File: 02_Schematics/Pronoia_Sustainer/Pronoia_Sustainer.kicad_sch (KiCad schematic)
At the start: 0 parts

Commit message: Initial start for Pronoia Schematic
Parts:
- added C1, C2: 10uF, symbol Device:C
- added C3, C4: 22uF, symbol Device:C
- added C5: 0.1uF, symbol Device:C
- added J1: J1_Bat, symbol Connector:Conn_01x02_Pin
- added J2: J2_Switch, symbol Connector:Conn_01x02_Pin
- added L1: 3.3uH, symbol Device:L
- added R1: 56.2k, symbol Device:R_US
- added R2: 10k, symbol Device:R_US
- added U1: TPS563201, Package_TO_SOT_SMD:SOT-23-6, symbol Regulator_Switching:TPS563201
- added U2: Teensy4.1, symbol teensy:Teensy4.1
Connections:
- new net: C1.1, C2.2, J2.2 (Pin_2), U1.3 (VIN), U1.5 (EN)
- new net: J1.1 (Pin_1), J2.1 (Pin_1)
- new net: R1.2, R2.1, U1.4 (VFB)
- new net: C5.1, L1.1, U1.2 (SW)
- new net: C5.2, U1.6 (VBST)
- new net +5V: C3.2, C4.1, L1.2, R1.1, U2.48 (VIN)
- new net GND: C1.2, C2.1, C3.1, C4.2, J1.2 (Pin_2), R2.2, U1.1 (GND), U2.47 (GND)
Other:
- company: (none) -> Walla Walla University
- title: (none) -> Pronoia Sustainer

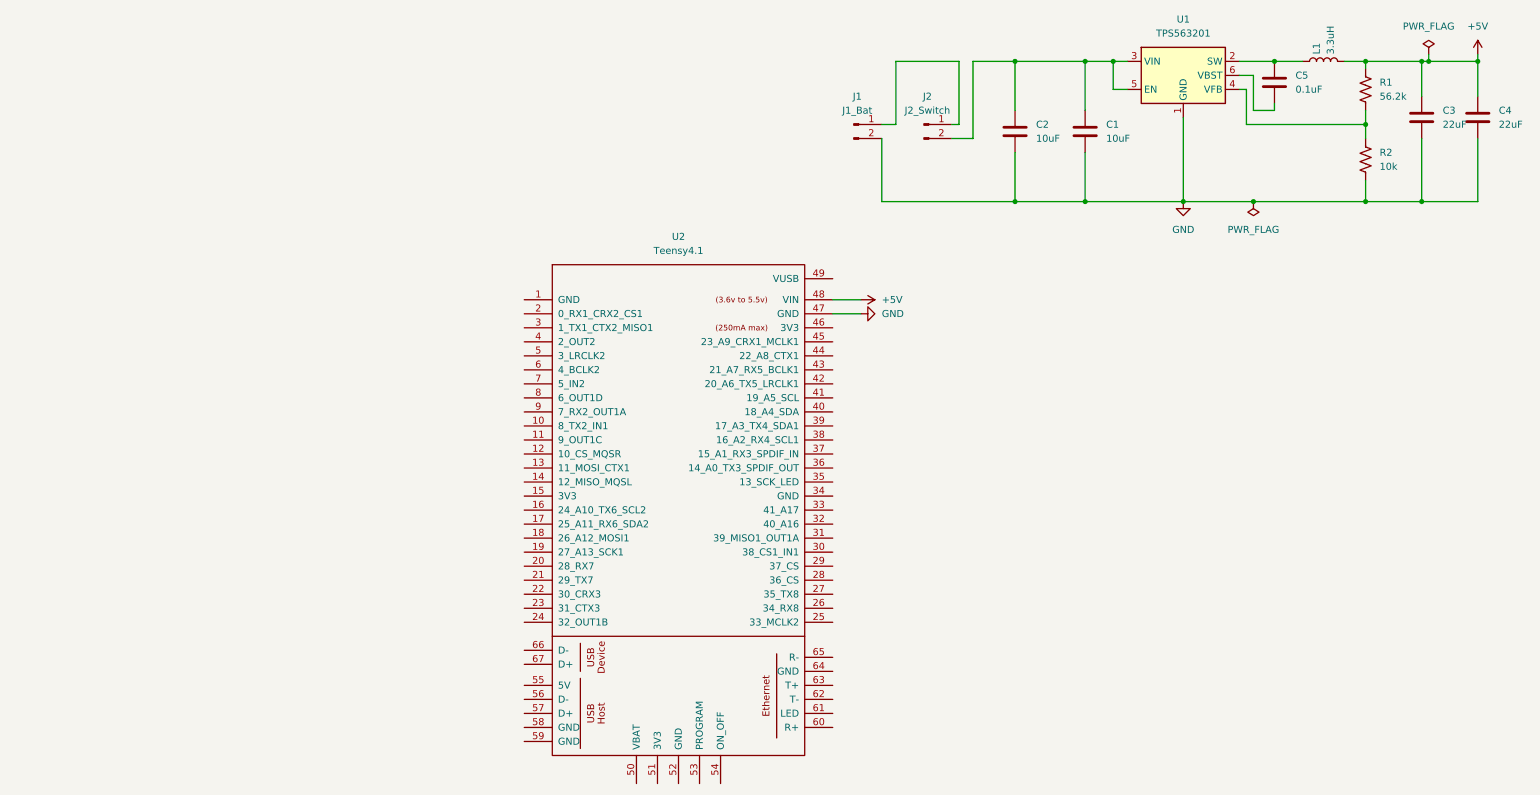
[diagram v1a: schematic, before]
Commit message: Added 1st Pyro Channel w/ Continuity Testing
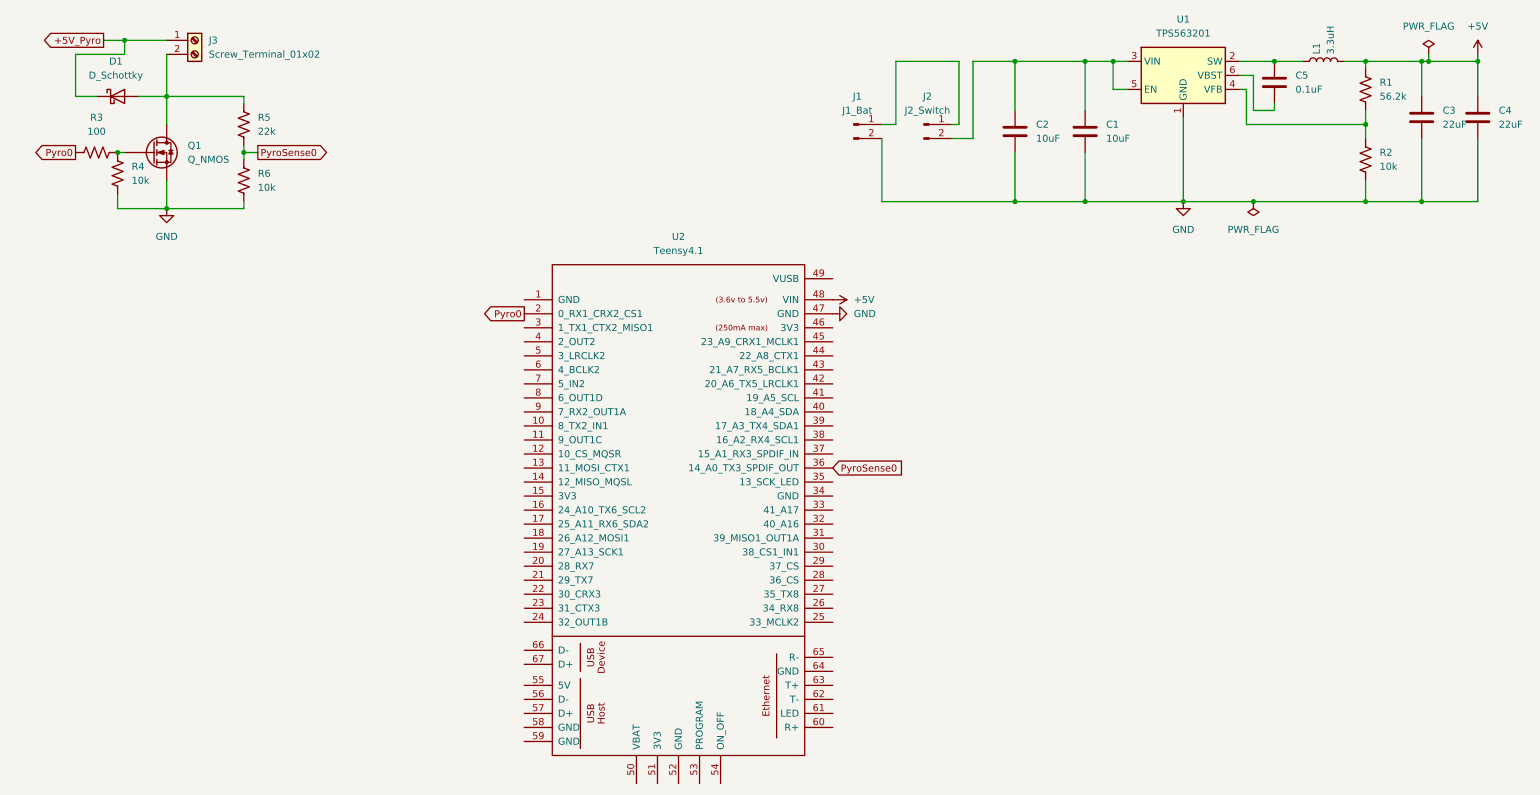
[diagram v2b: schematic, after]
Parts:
- added D1: D_Schottky, symbol Device:D_Schottky
- added J3: Screw_Terminal_01x02, TerminalBlock_Phoenix:TerminalBlock_Phoenix_MKDS-1,5-2-5.08_1x02_P5.08mm_Horizontal, symbol Connector:Screw_Terminal_01x02
- added Q1: Q_NMOS, Package_TO_SOT_SMD:SOT-23-3, symbol Device:Q_NMOS
- added R3: 100, symbol Device:R_US
- added R4, R6: 10k, symbol Device:R_US
- added R5: 22k, symbol Device:R_US
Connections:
- net GND: now also Q1.S, R4.2, R6.2
- net Pyro0: now reaches U2.2 (0_RX1_CRX2_CS1)
- net Pyro0: now also R3.1
- net PyroSense0: now reaches U2.36 (14_A0_TX3_SPDIF_OUT)
- net PyroSense0: now also R5.2, R6.1
- new net: D1.2 (A), J3.2 (Pin_2), Q1.D, R5.1
- new net: Q1.G, R3.2, R4.1
- new net +5V_Pyro: D1.1 (K), J3.1 (Pin_1)

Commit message: Added Servo Motor PWM Pin Headers and Electrolytic Capacitor
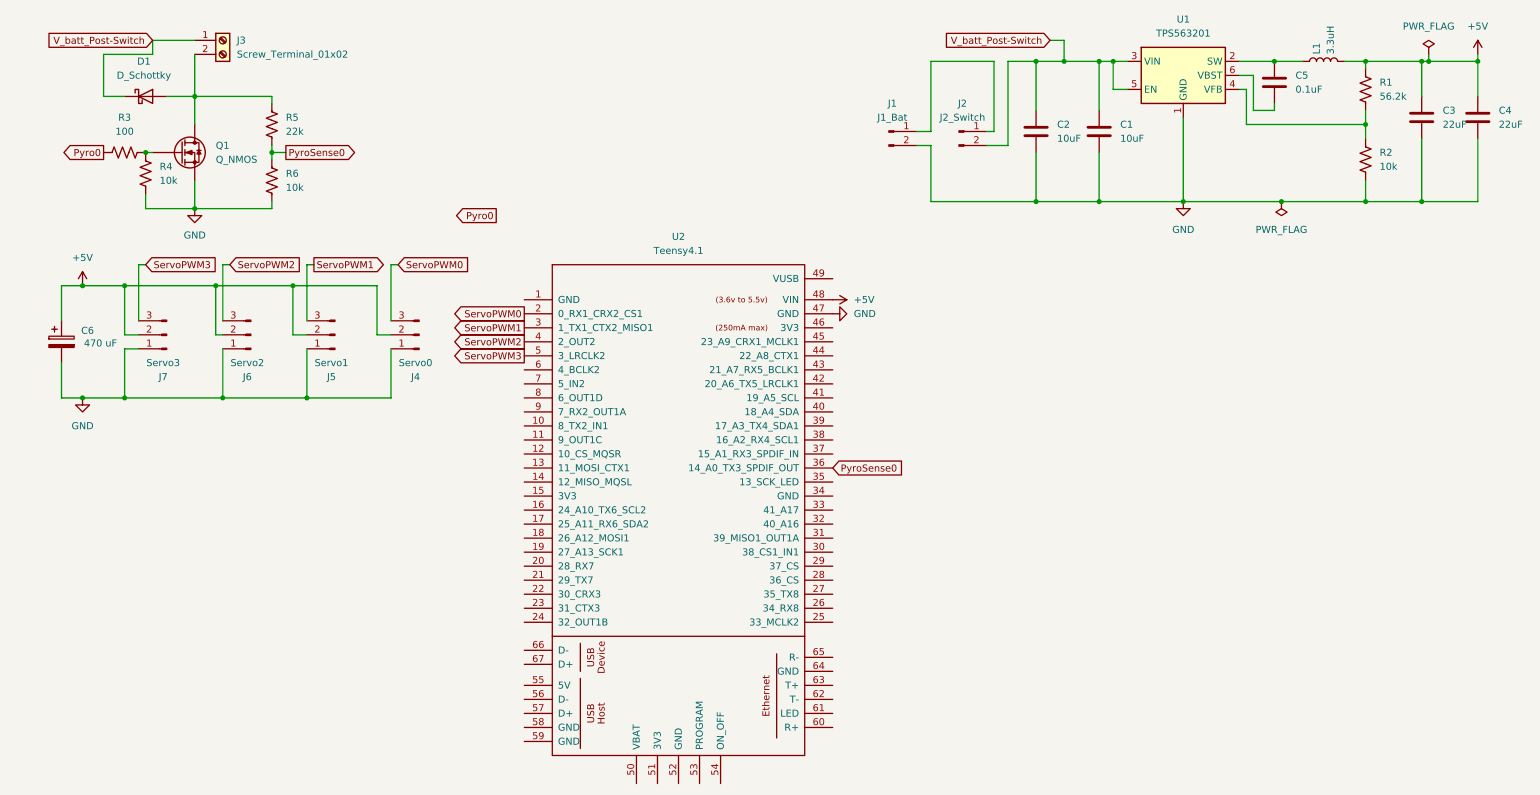
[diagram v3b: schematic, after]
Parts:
- added C6: 470 uF, symbol Device:C_Polarized
- added J4: Servo0, symbol Connector:Conn_01x03_Pin
- added J5: Servo1, symbol Connector:Conn_01x03_Pin
- added J6: Servo2, symbol Connector:Conn_01x03_Pin
- added J7: Servo3, symbol Connector:Conn_01x03_Pin
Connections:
- net +5V_Pyro is gone; now on net V_batt_Post-Switch: D1.1 (K), J3.1 (Pin_1)
- net +5V: now also C6.1, J4.2 (Pin_2), J5.2 (Pin_2), J6.2 (Pin_2), J7.2 (Pin_2)
- net GND: now also C6.2, J4.1 (Pin_1), J5.1 (Pin_1), J6.1 (Pin_1), J7.1 (Pin_1)
- net Pyro0: no longer U2.2 (0_RX1_CRX2_CS1)
- net V_batt_Post-Switch: now reaches C1.1, C2.2, J2.2 (Pin_2), U1.3 (VIN), U1.5 (EN)
- net ServoPWM1: now reaches U2.3 (1_TX1_CTX2_MISO1)
- net ServoPWM1: now also J5.3 (Pin_3)
- net ServoPWM2: now reaches U2.4 (2_OUT2)
- net ServoPWM2: now also J6.3 (Pin_3)
- net ServoPWM3: now reaches U2.5 (3_LRCLK2)
- net ServoPWM3: now also J7.3 (Pin_3)
- new net ServoPWM0: J4.3 (Pin_3), U2.2 (0_RX1_CRX2_CS1)
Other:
- moved on the sheet: C1, C2, D1, J1, J2, J3, Q1, R3, R4, R5, R6

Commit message: PyroChannel LTSpice Confirmation, Added LDO Regulator, Heirarchical Sheet
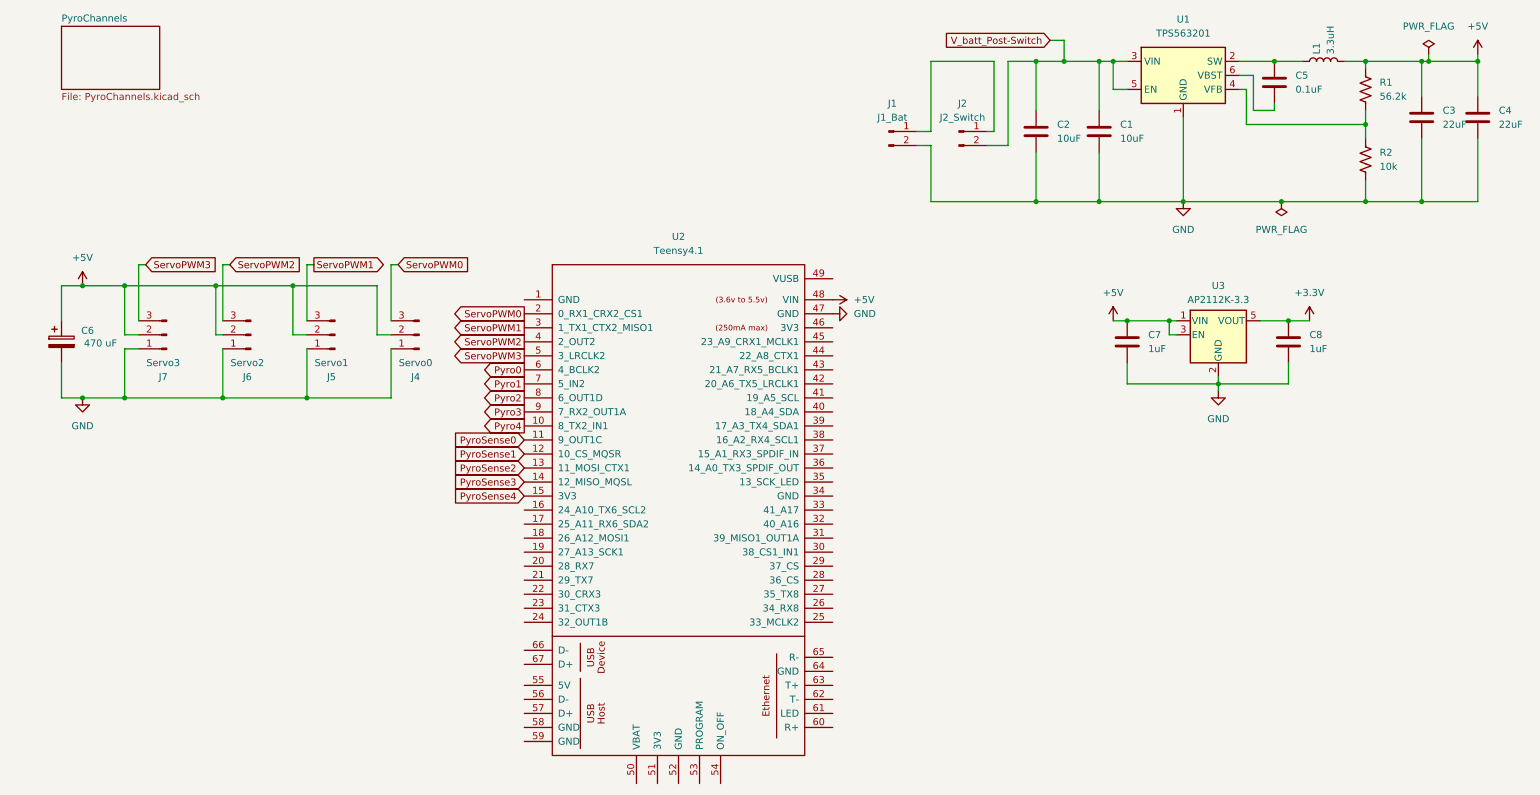
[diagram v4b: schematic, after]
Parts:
- removed D1: D_Schottky, symbol Device:D_Schottky
- removed J3: Screw_Terminal_01x02, TerminalBlock_Phoenix:TerminalBlock_Phoenix_MKDS-1,5-2-5.08_1x02_P5.08mm_Horizontal, symbol Connector:Screw_Terminal_01x02
- removed Q1: Q_NMOS, Package_TO_SOT_SMD:SOT-23-3, symbol Device:Q_NMOS
- removed R3: 100, symbol Device:R_US
- removed R4, R6: 10k, symbol Device:R_US
- removed R5: 22k, symbol Device:R_US
- added C7, C8: 1uF, symbol Device:C
- added U3: AP2112K-3.3, Package_TO_SOT_SMD:SOT-23-5, symbol Regulator_Linear:AP2112K-3.3
- U1: LCSC (none) -> C116592
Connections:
- net +5V: now also C7.2, U3.1 (VIN), U3.3 (EN)
- net GND: now also C7.1, C8.1, U3.2 (GND)
- net Pyro0: now also U2.6 (4_BCLK2)
- net PyroSense0: now also U2.11 (9_OUT1C); no longer U2.36 (14_A0_TX3_SPDIF_OUT)
- net Pyro4: now reaches U2.10 (8_TX2_IN1)
- net PyroSense1: now reaches U2.12 (10_CS_MQSR)
- net PyroSense2: now reaches U2.13 (11_MOSI_CTX1)
- net PyroSense3: now reaches U2.14 (12_MISO_MQSL)
- net PyroSense4: now reaches U2.15 (3V3)
- net Pyro1: now reaches U2.7 (5_IN2)
- net Pyro2: now reaches U2.8 (6_OUT1D)
- net Pyro3: now reaches U2.9 (7_RX2_OUT1A)
- new net +3.3V: C8.2, U3.5 (VOUT)
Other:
- added sheet PyroChannels (PyroChannels.kicad_sch)

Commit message: Added footprints to all placed symbols
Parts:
- removed C1, C2: 10uF, symbol Device:C
- removed C3, C4: 22uF, symbol Device:C
- removed C5: 0.1uF, symbol Device:C
- removed C7, C8: 1uF, symbol Device:C
- removed J1: J1_Bat, symbol Connector:Conn_01x02_Pin
- removed J2: J2_Switch, symbol Connector:Conn_01x02_Pin
- removed R1: 56.2k, symbol Device:R_US
- removed R2: 10k, symbol Device:R_US
- added C1, C2: 10uF, PCM_JLCPCB:C_1206, symbol PCM_JLCPCB-Capacitors:1206,10uF
- added C3, C4: 22uF, PCM_JLCPCB:C_0805, symbol PCM_JLCPCB-Capacitors:0805,22uF
- added C5: 100nF, PCM_JLCPCB:C_1206, symbol PCM_JLCPCB-Capacitors:1206,100nF
- added C7, C8: 1uF, PCM_JLCPCB:C_0603, symbol PCM_JLCPCB-Capacitors:0603,1uF
- added J1: XT30PW-M, XT30PW-M:AMASS_XT30PW-M, symbol XT30PW-M:XT30PW-M
- added J2: Screw_Terminal_01x02, TerminalBlock_Phoenix:TerminalBlock_Phoenix_MKDS-1,5-2-5.08_1x02_P5.08mm_Horizontal, symbol Connector:Screw_Terminal_01x02
- added R1: 49.9kΩ, PCM_JLCPCB:R_0805, symbol PCM_JLCPCB-Resistors:0805,49.9kΩ
- added R2: 9.1kΩ, PCM_JLCPCB:R_0805, symbol PCM_JLCPCB-Resistors:0805,9.1kΩ
- C6: footprint (none) -> Capacitor_SMD:CP_Elec_8x10; LCSC (none) -> C970706
- J4: footprint (none) -> Connector_PinHeader_2.54mm:PinHeader_1x03_P2.54mm_Vertical
- J5: value Servo1 -> Servo0; footprint (none) -> Connector_PinHeader_2.54mm:PinHeader_1x03_P2.54mm_Vertical
- J6: value Servo2 -> Servo0; footprint (none) -> Connector_PinHeader_2.54mm:PinHeader_1x03_P2.54mm_Vertical
- J7: value Servo3 -> Servo0; footprint (none) -> Connector_PinHeader_2.54mm:PinHeader_1x03_P2.54mm_Vertical
- L1: footprint (none) -> Inductor_SMD:L_Bourns-SRN8040_8x8.15mm; LCSC (none) -> C780188
- U2: footprint (none) -> teensy.pretty-master:Teensy41
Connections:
- net +3.3V: now also C8.1
- net +5V: now also C3.1, C4.1, C7.1, R1.1
- net GND: now also C1.2, C2.2, C3.2, C4.2, C7.2, C8.2, J1.N, R2.2
- net V_batt_Post-Switch: now also C1.1, C2.1, J2.1 (Pin_1)
- net at U1.4 (VFB): now also R1.2, R2.1
- net at L1.1, U1.2 (SW): now also C5.1
- net at U1.6 (VBST): now also C5.2
- new net: J1.P, J2.2 (Pin_2)
